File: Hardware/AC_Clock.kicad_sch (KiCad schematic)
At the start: 0 parts

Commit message: Add Power circuits and pulse input
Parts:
- added C1: 10u, symbol Device:C_Small
- added C2: 22u, symbol Device:C_Small
- added D1: ABS2, Diode_SMD:Diode_Bridge_Diotec_ABS, symbol Diode_Bridge:ABS2
- added R1, R2: 1k, symbol Device:R
- added T1: 10:1, symbol Device:Transformer_1P_1S
- added U1: AZ1117-5.0, Package_TO_SOT_SMD:SOT-223-3_TabPin2, symbol Regulator_Linear:AZ1117-5.0
- added U2: LTV-817S, Package_DIP:SMDIP-6_W9.53mm_Clearance8mm, symbol Isolator:LTV-817S
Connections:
- new net: R1.2, U2.2
- new net +5V: C2.1, U1.2 (VO), U2.4
- new net AC: T1.1 (AA)
- new net AC_12+: D1.4, T1.4 (SB), U2.1
- new net AC_12-: D1.3, R1.1, T1.3 (SA)
- new net Earth: T1.2 (AB)
- new net GND: C1.2, C2.2, D1.2 (-), R2.2, U1.1 (GND)
- new net Pulse: R2.1, U2.3
- new net VBUS: C1.1, D1.1 (+), U1.3 (VI)
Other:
- note added: "5V PWS"
- note added: "AC in"
- note added: "Optocoupler -> 60Hz count"

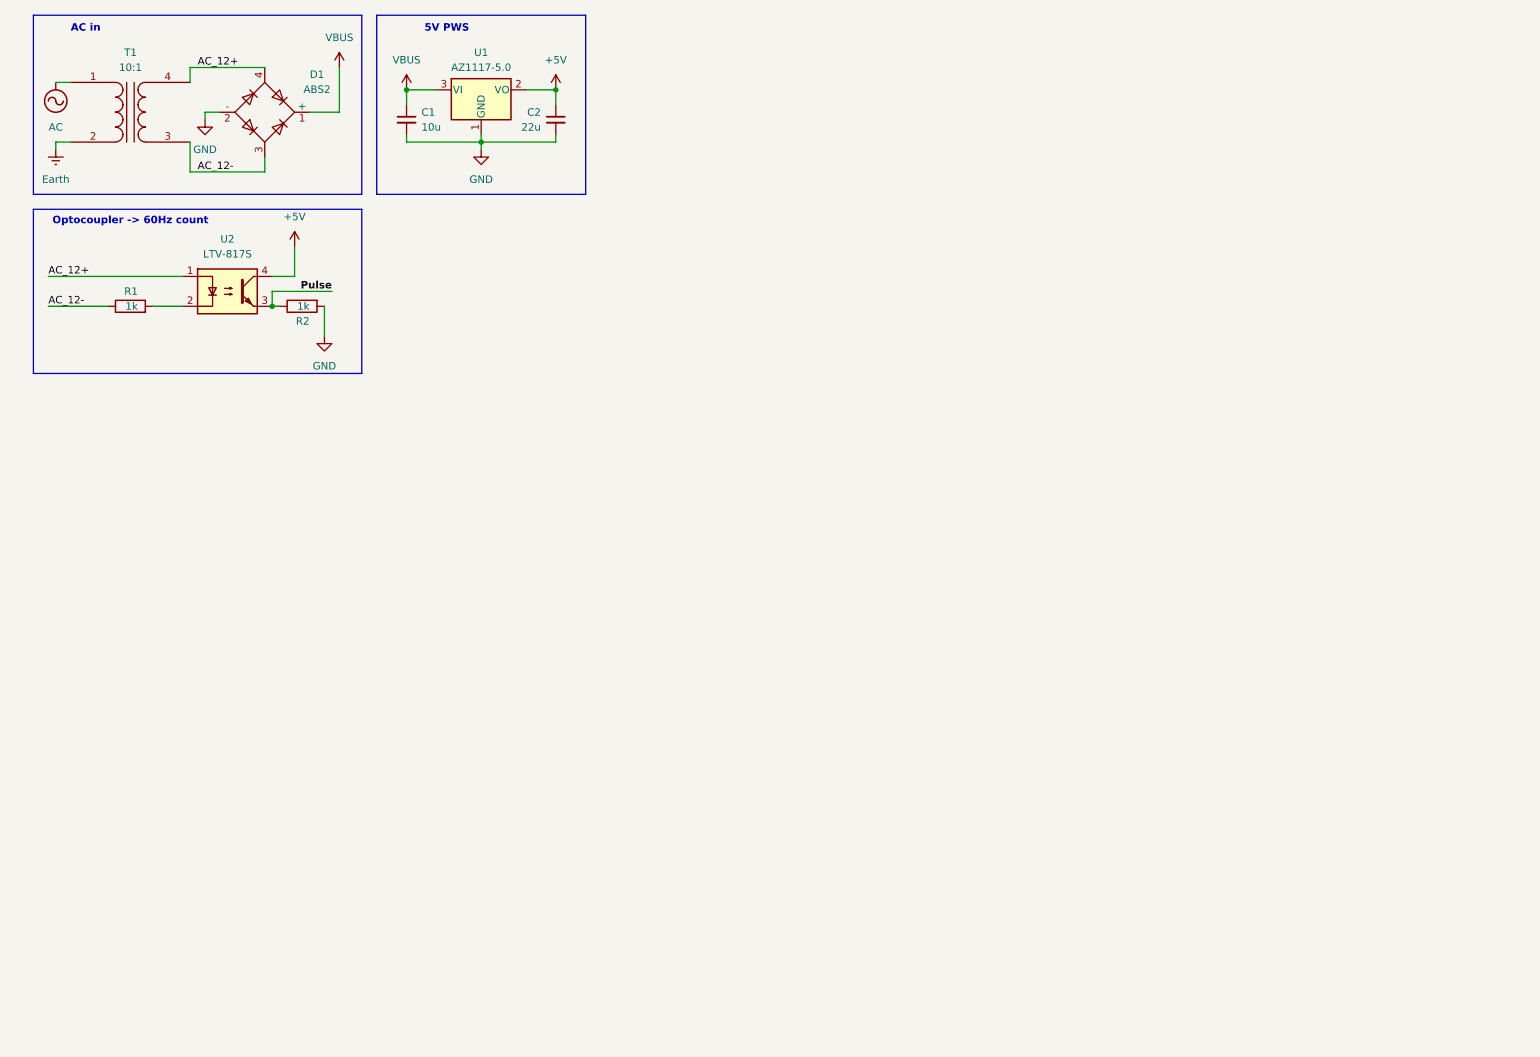
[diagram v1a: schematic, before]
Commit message: Add frequency divider (60Hz to min) and minutes counter
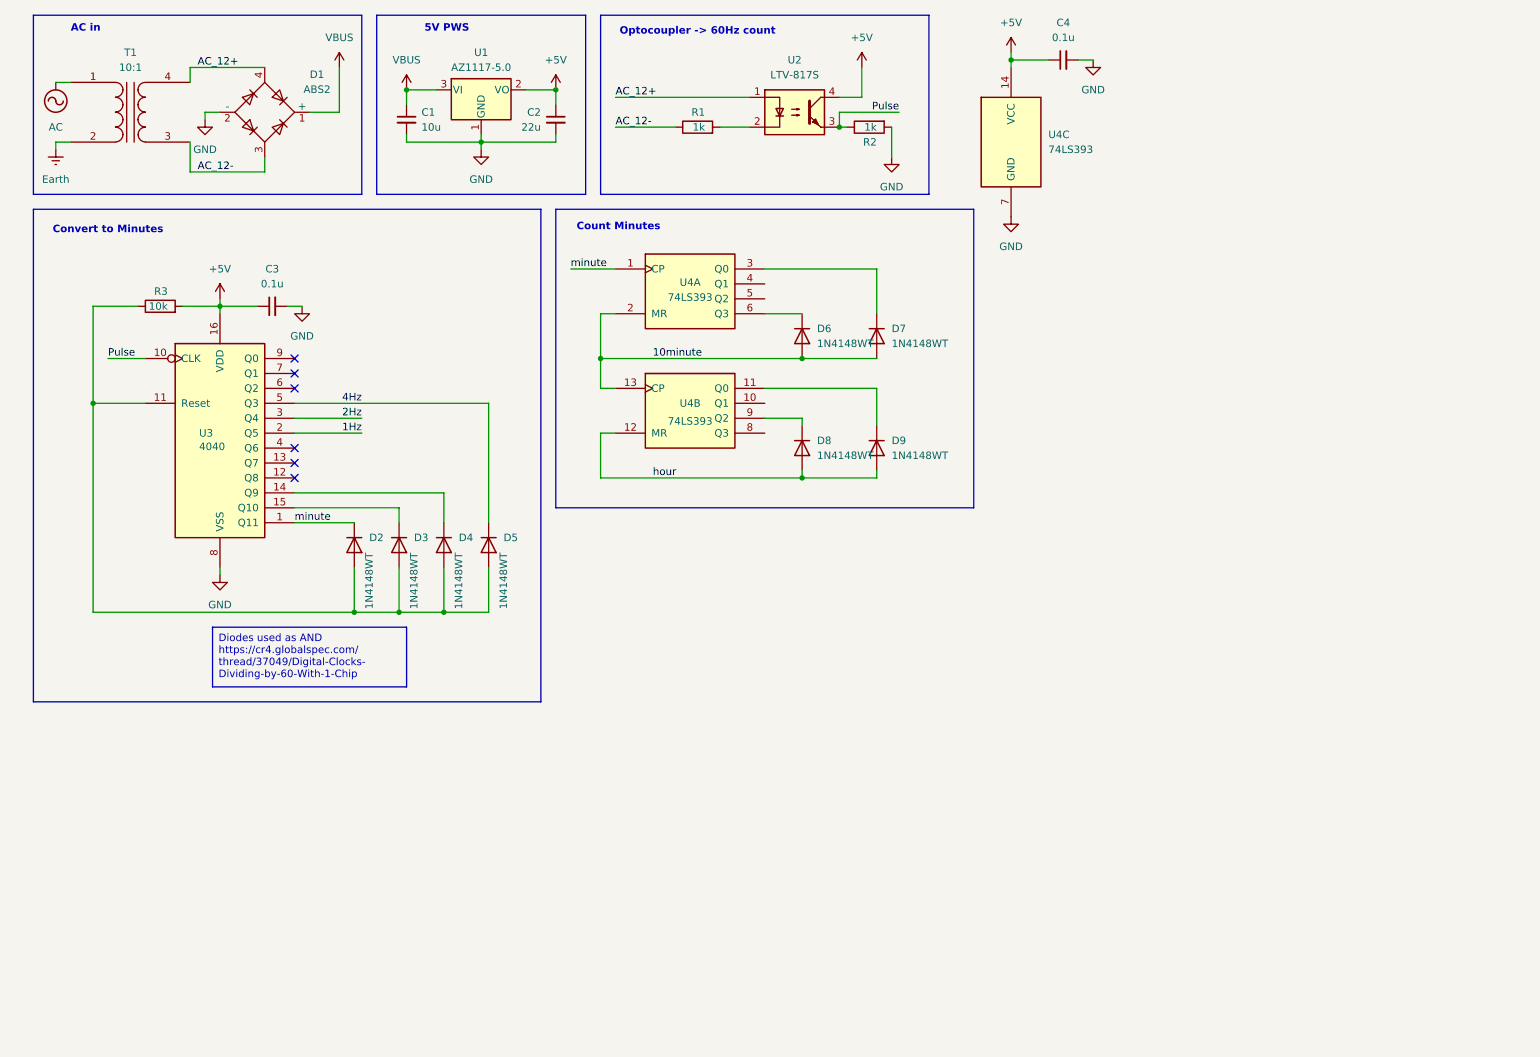
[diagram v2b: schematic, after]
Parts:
- added C3, C4: 0.1u, symbol Device:C_Small
- added D2, D3, D4, D5, D6, D7, D8, D9: 1N4148WT, Diode_SMD:D_SOD-523, symbol Diode:1N4148WT
- added R3: 10k, symbol Device:R
- added U3: 4040, symbol 4xxx:4040
- added U4: 74LS393, symbol 74xx:74LS393
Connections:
- net +5V: now also C3.1, C4.1, R3.2, U3.16 (VDD), U4.14 (VCC)
- net GND: now also C3.2, C4.2, U3.8 (VSS), U4.7 (GND)
- net Pulse: now also U3.10 (CLK)
- new net: D2.2 (A), D3.2 (A), D4.2 (A), D5.2 (A), R3.1, U3.11 (Reset)
- new net: D9.1 (K), U4.11 (Q0)
- new net: D4.1 (K), U3.14 (Q9)
- new net: D6.1 (K), U4.6 (Q3)
- new net: D3.1 (K), U3.15 (Q10)
- new net: D8.1 (K), U4.9 (Q2)
- new net: D7.1 (K), U4.3 (Q0)
- new net 10minute: D6.2 (A), D7.2 (A), U4.13 (CP), U4.2 (MR)
- new net 1Hz: U3.2 (Q5)
- new net 2Hz: U3.3 (Q4)
- new net 4Hz: D5.1 (K), U3.5 (Q3)
- new net hour: D8.2 (A), D9.2 (A), U4.12 (MR)
- new net minute: D2.1 (K), U3.1 (Q11), U4.1 (CP)
- no-connect marks 0 -> 6
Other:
- note added: "Convert to Minutes"
- note added: "Count Minutes"
- moved on the sheet: R1, R2, U2

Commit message: Add Hour Counter and display driver for minutes and ten minutes
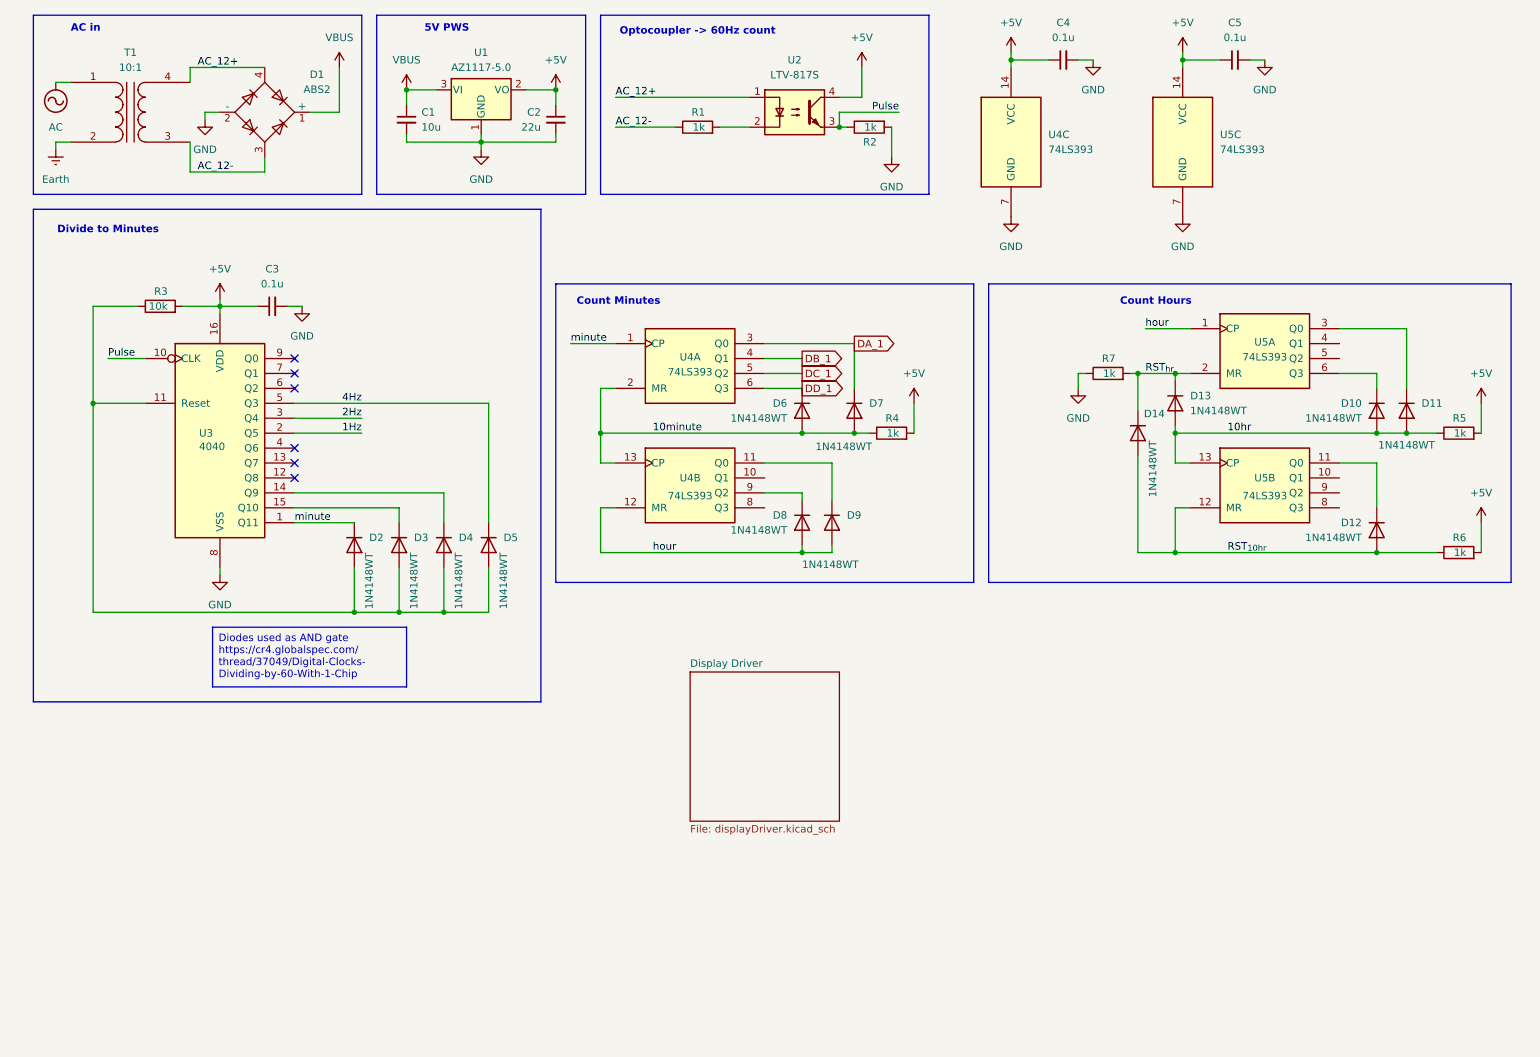
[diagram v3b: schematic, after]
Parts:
- added C5: 0.1u, symbol Device:C_Small
- added D10, D11, D12, D13, D14: 1N4148WT, Diode_SMD:D_SOD-523, symbol Diode:1N4148WT
- added R4, R5, R6, R7: 1k, symbol Device:R
- added U5: 74LS393, symbol 74xx:74LS393
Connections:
- net +5V: now also C5.1, R4.2, R5.2, R6.2, U5.14 (VCC)
- net 10minute: now also R4.1
- net GND: now also C5.2, R7.1, U5.7 (GND)
- net hour: now also U5.1 (CP)
- net DD_1: now reaches D6.1 (K), U4.6 (Q3)
- net DA_1: now reaches D7.1 (K), U4.3 (Q0)
- net DB_1: now reaches U4.4 (Q1)
- net DC_1: now reaches U4.5 (Q2)
- new net: D12.1 (K), U5.11 (Q0)
- new net: D11.1 (K), U5.3 (Q0)
- new net: D10.1 (K), U5.6 (Q3)
- new net 10hr: D10.2 (A), D11.2 (A), D13.2 (A), R5.1, U5.13 (CP)
- new net RST_{10hr}: D12.2 (A), D14.2 (A), R6.1, U5.12 (MR)
- new net RST_{hr}: D13.1 (K), D14.1 (K), R7.2, U5.2 (MR)
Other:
- added sheet Display Driver (displayDriver.kicad_sch)
- note added: "Count Hours"
- note added: "Divide to Minutes"
- note removed: "Convert to Minutes"
- moved on the sheet: D6, D7, D8, D9, U4A, U4B

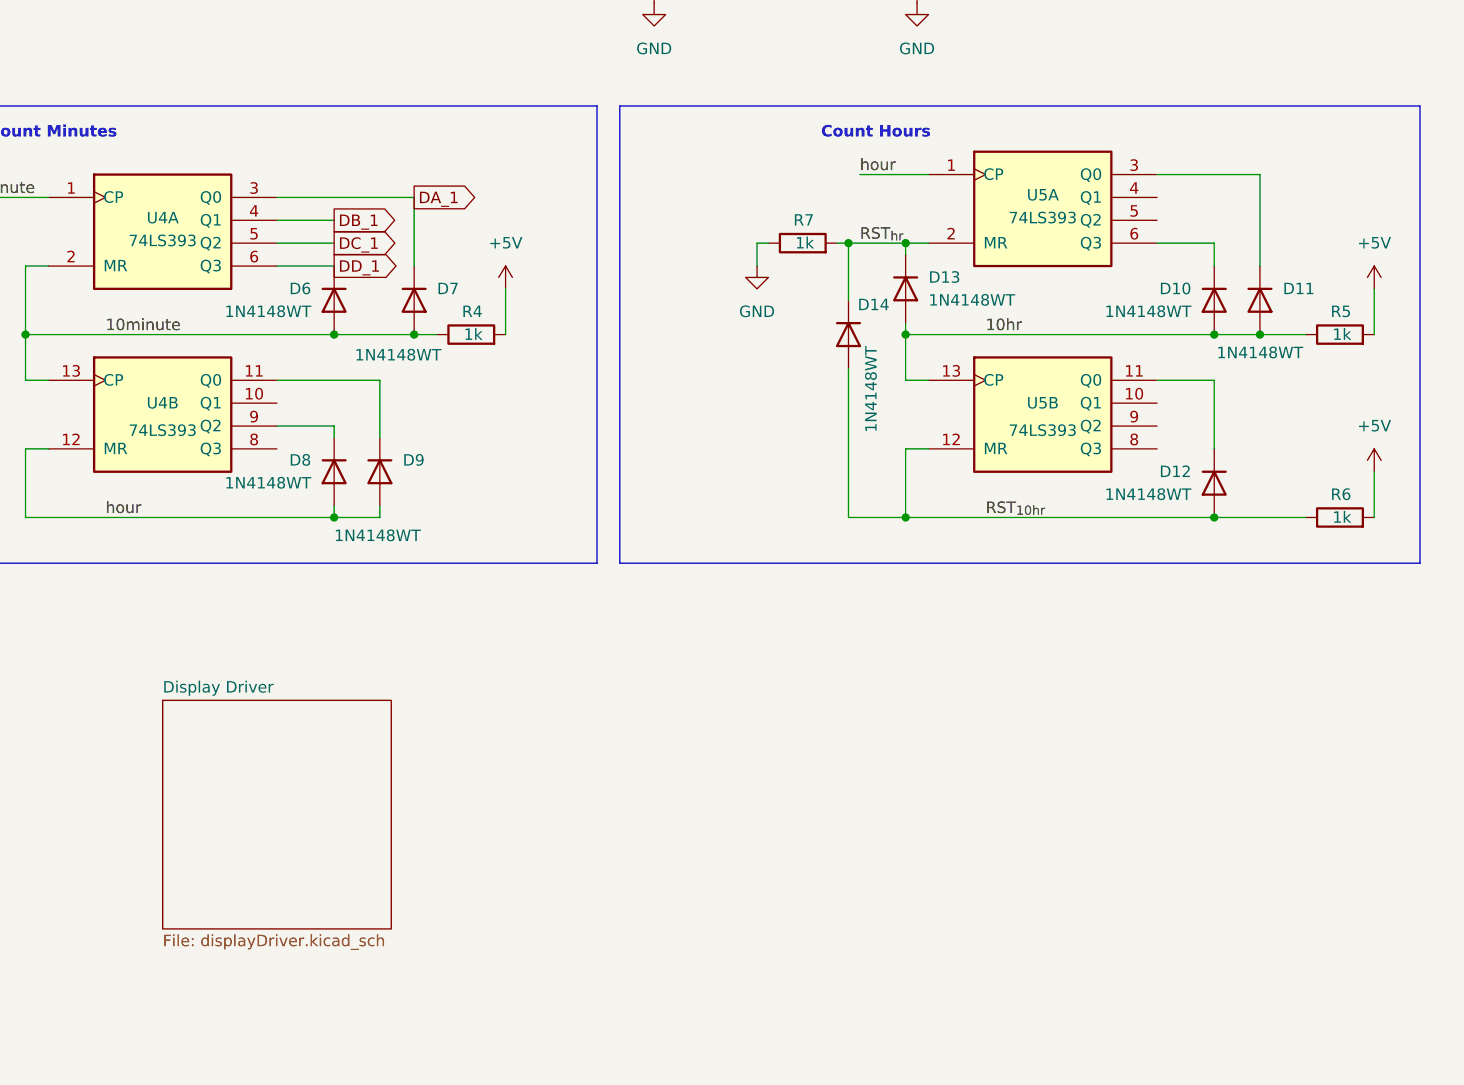
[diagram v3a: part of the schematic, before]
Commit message: Add in BCD net-labels and clean up drawings.
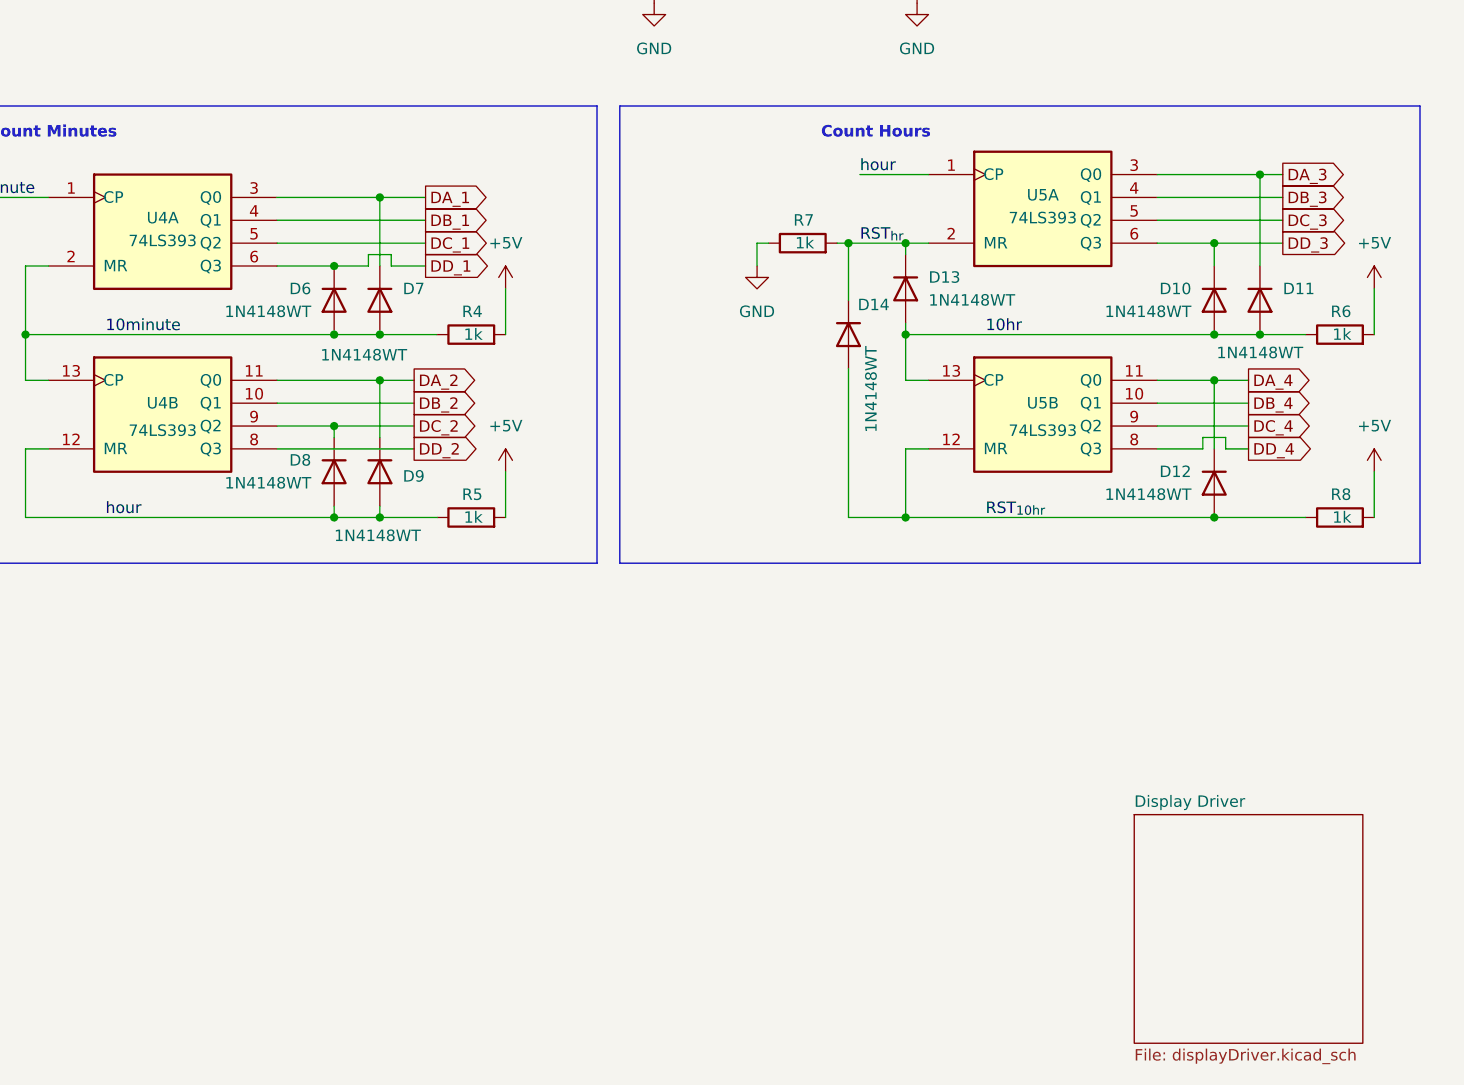
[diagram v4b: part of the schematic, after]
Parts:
- added R5: 1k, symbol Device:R
- renumbered R5 to R6, R6 to R8
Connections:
- net +5V: now also R5.2
- net hour: now also R5.1
- net DA_4: now reaches D12.1 (K), U5.11 (Q0)
- net DA_2: now reaches D9.1 (K), U4.11 (Q0)
- net DA_3: now reaches D11.1 (K), U5.3 (Q0)
- net DC_2: now reaches D8.1 (K), U4.9 (Q2)
- net DB_2: now reaches U4.10 (Q1)
- net DD_2: now reaches U4.8 (Q3)
- net DD_3: now reaches D10.1 (K), U5.6 (Q3)
- net DB_3: now reaches U5.4 (Q1)
- net DC_3: now reaches U5.5 (Q2)
- net DB_4: now reaches U5.10 (Q1)
- net DD_4: now reaches U5.8 (Q3)
- net DC_4: now reaches U5.9 (Q2)
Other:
- moved on the sheet: D7
